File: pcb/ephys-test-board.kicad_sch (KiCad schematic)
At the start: 9 parts, among them J1 10129383-910002ALF, J8 BM03B-SRSS-TB

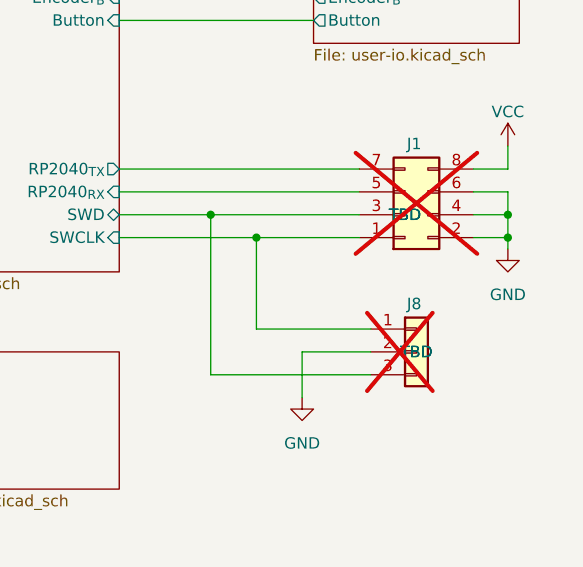
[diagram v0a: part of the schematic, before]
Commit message: BOM completed
- OEPSPN & MPN fully complete
- .csv BOM file updated
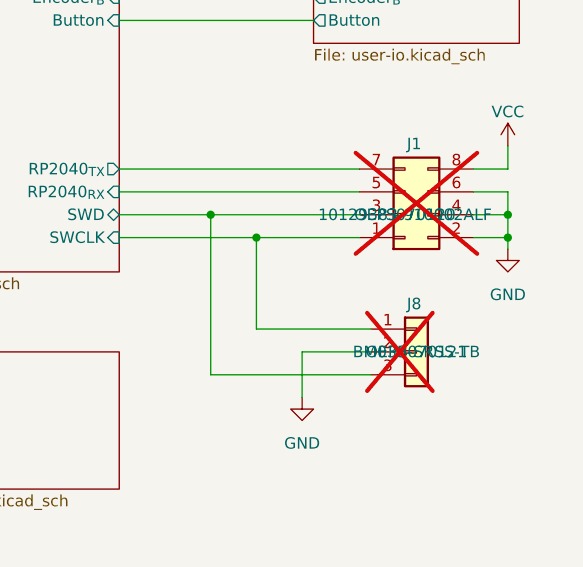
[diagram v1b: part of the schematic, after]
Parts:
- J1: value 10129383-910002ALF -> DNP; MPN TBD -> 10129383-910002ALF; OEPSPN TBD -> OEPS070120
- J8: value BM03B-SRSS-TB -> DNP; MPN TBD -> BM03B-SRSS-TB; OEPSPN TBD -> OEPS070121
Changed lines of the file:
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@@
 			)
 		)
-		(property "Value" "10129383-910002ALF"
+		(property "Value" "DNP"
 			(at 252.73 111.76 0)
 			(effects
@@
 			)
 		)
-		(property "MPN" "TBD"
+		(property "MPN" "10129383-910002ALF"
 			(at 251.46 97.79 0)
 			(effects
@@
 			)
 		)
-		(property "OEPSPN" "TBD"
+		(property "OEPSPN" "OEPS070120"
 			(at 251.46 97.79 0)
 			(effects
@@
 			)
 		)
-		(property "Value" "BM03B-SRSS-TB"
+		(property "Value" "DNP"
 			(at 252.73 119.38 0)
 			(effects
@@
 			)
 		)
-		(property "MPN" "TBD"
+		(property "MPN" "BM03B-SRSS-TB"
 			(at 252.73 113.03 0)
 			(effects
@@
 			)
 		)
-		(property "OEPSPN" "TBD"
+		(property "OEPSPN" "OEPS070121"
 			(at 252.73 113.03 0)
 			(effects
